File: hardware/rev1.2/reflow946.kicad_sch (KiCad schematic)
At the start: 47 parts, among them J1 VH-2A, J2 VH-3A2, J3 VH-3A2, J4 XH-A2, J5 HDR-M-2.54_2x3, Q1 BTA16-600BRG, Q2 MMBT3906, Q3 MMBT3906, Q4 MMBT3906, SW1 SW_Push, SW2 SW_Push, SW3 SW_Push, U1 MOC3041M, U2 ESP32-WROOM-32U, U3 MAX31855KASA, U4 AMS1117-3.3

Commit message: Fork to randware R2 variant
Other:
- company: Arnaud Durand -> Randware • Trent Rand

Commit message: rev2 schematic: J6 display pogo interface + J7 probe breakout
- Rename segment nets a/b -> SDA/SCL (IO17/IO22), trim dead tails
- J6 Conn_01x04 pogo target: 3V3/GND/SDA/SCL, R21/R22 4.7k pull-ups
- J7 Conn_01x06 breakout for external TC amp:
  CLK(IO14)/MISO(IO12) shared SPI, CS_EXT(IO4), TC_ADC(SENSOR_VP)
- Free IO4 & SENSOR_VP no-connects; DS1 7-seg -> DNP
- Remove orphaned a/b stubs, bus entries, dead DS1-side labels
- ERC: no new functional violations vs baseline; netlist verified
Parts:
- added J6: OLED_POGO, Connector_PinHeader_2.54mm:PinHeader_1x04_P2.54mm_Vertical, symbol Connector_Generic:Conn_01x04
- added J7: PROBE_BRK, Connector_PinHeader_2.54mm:PinHeader_1x06_P2.54mm_Vertical, symbol Connector_Generic:Conn_01x06
- added R21, R22: 4.7k, Resistor_SMD:R_0603_1608Metric_Pad0.98x0.95mm_HandSolder, symbol Device:R
- DS1: now not fitted
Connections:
- net +3.3V: now also J6.1 (Pin_1), J7.1 (Pin_1), R21.1, R22.1
- net CLK: now also J7.3 (Pin_3)
- net GND: now also J6.2 (Pin_2), J7.2 (Pin_2)
- net MISO: now also J7.4 (Pin_4)
- net CS_EXT: now reaches U2.26 (IO4)
- net CS_EXT: now also J7.5 (Pin_5)
- net TC_ADC: now reaches U2.4 (SENSOR_VP)
- net TC_ADC: now also J7.6 (Pin_6)
- net a: no longer names the net of R17.1
- net a: no longer U2.28 (IO17)
- net b: no longer names the net of R15.1
- net b: no longer U2.36 (IO22)
- new net SCL: J6.4 (Pin_4), R22.2, U2.36 (IO22)
- new net SDA: J6.3 (Pin_3), R21.2, U2.28 (IO17)

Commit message: rev2: J6 -> 8-pin TFT SPI header, embedded U6 second MAX31855 + EXT_TC terminal
Display path (ST7789V3 1.47in 172x320 IPS):
- J6 Conn_01x08: 3V3/GND/CS(IO23)/DC(IO16)/RST(IO13)/SCK(IO18)/MOSI(IO19)/BLK(IO5)
- Six freed segment GPIOs relabeled to TFT_* nets; dangling tails trimmed
- Q3 + R19 DNP to free IO18; DS1-side dead labels/stubs/bus entries removed

External probe subsystem:
- U6 MAX31855KASA clone sharing CLK/MISO, CS on IO4 (CS_EXT)
- J8 Phoenix MPT screw terminal + FB3/FB4 beads + C7 filter (mirrors U3 pattern)
- SENSOR_VP broken out as TC_ADC; J7 breakout retained

I2C expansion bus (IO17/IO22) kept with R21/R22 pull-ups.

ERC: zero new functional violations vs baseline (38 vs 49 findings;
net_not_bus_member improved). Netlist: all connectivity assertions pass,
including triac/button paths byte-identical to HEAD.
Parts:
- removed J6: OLED_POGO, Connector_PinHeader_2.54mm:PinHeader_1x04_P2.54mm_Vertical, symbol Connector_Generic:Conn_01x04
- added C7: 0.01u, Capacitor_SMD:C_0805_2012Metric_Pad1.18x1.45mm_HandSolder, symbol Device:C
- added FB3, FB4: FerriteBead, Resistor_SMD:R_0603_1608Metric_Pad0.98x0.95mm_HandSolder, symbol Device:FerriteBead
- added J6: TFT_1.47, Connector_PinHeader_2.54mm:PinHeader_1x08_P2.54mm_Vertical, symbol Connector_Generic:Conn_01x08
- added J8: EXT_TC, TerminalBlock_Phoenix:TerminalBlock_Phoenix_MPT-0,5-2-2.54_1x02_P2.54mm_Horizontal, symbol Connector_Generic:Conn_01x02
- added U6: MAX31855KASA, Package_SO:SOIC-8_3.9x4.9mm_P1.27mm, symbol Sensor_Temperature:MAX31855KASA
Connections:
- net +3.3V: now also J6.1 (Pin_1), U6.4 (VCC)
- net CLK: now also U6.5 (SCK)
- net CS_EXT: now also U6.6 (~{CS})
- net GND: now also J6.2 (Pin_2), U6.1 (GND)
- net MISO: now also U6.7 (SO)
- net c: no longer names the net of R13.1
- net c: no longer U2.31 (IO19)
- net d: no longer names the net of R11.1
- net d: no longer U2.27 (IO16)
- net d2: no longer names the net of R19.1
- net d2: no longer U2.30 (IO18)
- net dp: no longer names the net of R12.1
- net dp: no longer U2.29 (IO5)
- net f: no longer names the net of R16.1
- net f: no longer U2.37 (IO23)
- net g: no longer names the net of R14.1
- net g: no longer U2.16 (IO13)
- new net: C7.1, FB3.1, U6.3 (T+)
- new net: C7.2, FB4.1, U6.2 (T-)
- new net: FB3.2, J8.1 (Pin_1)
- new net: FB4.2, J8.2 (Pin_2)
- new net TFT_BLK: J6.8 (Pin_8), U2.29 (IO5)
- new net TFT_CS: J6.3 (Pin_3), U2.37 (IO23)
- new net TFT_DC: J6.4 (Pin_4), U2.27 (IO16)
- new net TFT_MOSI: J6.7 (Pin_7), U2.31 (IO19)
- new net TFT_RST: J6.5 (Pin_5), U2.16 (IO13)
- new net TFT_SCK: J6.6 (Pin_6), U2.30 (IO18)
- no-connect marks 11 -> 17

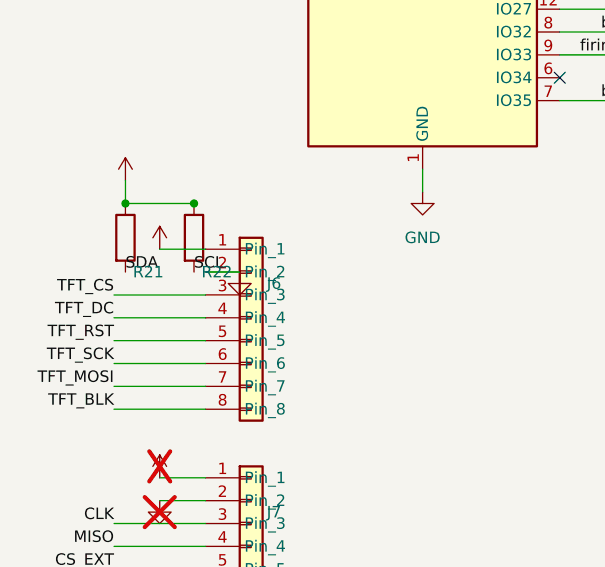
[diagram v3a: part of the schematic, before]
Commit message: rev2: route J6 GND stub leftward (was ending on connector body edge)
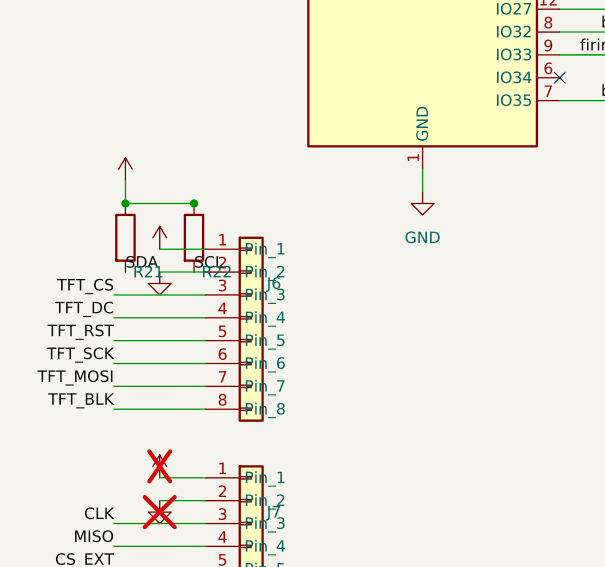
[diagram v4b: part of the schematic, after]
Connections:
- net SCL is gone; now on net GND: R22.2, U2.36 (IO22)
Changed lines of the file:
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@@
 	(wire
 		(pts
-			(xy 29.21 162.56) (xy 33.02 162.56)
+			(xy 29.21 162.56) (xy 24.13 162.56)
 		)
 		(stroke
@@
 	(symbol
 		(lib_id "power:GND")
-		(at 33.02 162.56 0)
+		(at 24.13 162.56 0)
 		(unit 1)
 		(body_style 1)
@@
 		)
 		(property "Footprint" ""
-			(at 33.02 162.56 0)
+			(at 24.13 162.56 0)
 			(hide yes)
 			(show_name no)
@@
 		)
 		(property "Datasheet" ""
-			(at 33.02 162.56 0)
+			(at 24.13 162.56 0)
 			(hide yes)
 			(show_name no)
@@
 		)
 		(property "Description" ""
-			(at 33.02 162.56 0)
+			(at 24.13 162.56 0)
 			(hide yes)
 			(show_name no)

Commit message: rev2: fix stray DNP flags on J7 power symbols; DNP Q3/R19 properly; relocate I2C pull-ups
- #PWR0118/#PWR0120 carried stray dnp=yes (collateral of an earlier
  unbounded rindex in the Q3/R19 DNP pass) -> cleared
- Q3 + R19 now genuinely DNP, freeing IO18 for TFT_SCK
- R21/R22 pull-up mini-circuit moved +21.59mm clear of J6's rail stubs
  (SCL label anchor previously sat on J6's GND stub path - nets verified
  separate but one edit away from shorting)
- ERC 38 (== baseline classes), netlist assertions all pass
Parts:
- Q3, R19: now not fitted
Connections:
- net GND: no longer R22.2, U2.36 (IO22)
- new net SCL: R22.2, U2.36 (IO22)
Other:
- moved on the sheet: R21, R22
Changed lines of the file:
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@@
 	)
 	(label "SDA"
-		(at 20.32 162.56 0)
+		(at 41.91 162.56 0)
 		(effects
 			(font
@@
 	)
 	(label "SCL"
-		(at 27.94 162.56 0)
+		(at 49.53 162.56 0)
 		(effects
 			(font
@@
 	(wire
 		(pts
-			(xy 20.32 152.4) (xy 20.32 154.94)
+			(xy 41.91 152.4) (xy 41.91 154.94)
 		)
 		(stroke
@@
 	(wire
 		(pts
-			(xy 20.32 154.94) (xy 27.94 154.94)
+			(xy 41.91 154.94) (xy 49.53 154.94)
 		)
 		(stroke
@@
 	)
 	(junction
-		(at 20.32 154.94)
+		(at 41.91 154.94)
 		(diameter 0)
 		(color 0 0 0 0)
 	)
 	(junction
-		(at 27.94 154.94)
+		(at 49.53 154.94)
 		(diameter 0)
 		(color 0 0 0 0)
@@
 		(on_board yes)
 		(in_pos_files yes)
-		(dnp no)
+		(dnp yes)
 		(property "Reference" "R19"
 			(at 180.34 33.02 90)
@@
 		(on_board yes)
 		(in_pos_files yes)
-		(dnp no)
+		(dnp yes)
 		(fields_autoplaced yes)
 		(property "Reference" "Q3"
@@
 	(symbol
 		(lib_id "Device:R")
-		(at 20.32 158.75 0)
+		(at 41.91 158.75 0)
 		(unit 1)
 		(body_style 1)
@@
 		(fields_autoplaced yes)
 		(property "Reference" "R21"
-			(at 22.86 162.56 0)
+			(at 44.45 162.56 0)
 			(show_name no)
 			(do_not_autoplace no)
@@
 		)
 		(property "Value" "4.7k"
-			(at 22.86 154.94 0)
+			(at 44.45 154.94 0)
 			(hide yes)
 			(show_name no)
@@
 		)
 		(property "Footprint" "Resistor_SMD:R_0603_1608Metric_Pad0.98x0.95mm_HandSolder"
-			(at 20.32 158.75 0)
+			(at 41.91 158.75 0)
 			(hide yes)
 			(show_name no)
@@
 		)
 		(property "Datasheet" "~"
-			(at 20.32 158.75 0)
+			(at 41.91 158.75 0)
 			(hide yes)
 			(show_name no)
@@
 		)
 		(property "Description" ""
-			(at 20.32 158.75 0)
+			(at 41.91 158.75 0)
 			(hide yes)
 			(show_name no)
@@
 	(symbol
 		(lib_id "Device:R")
-		(at 27.94 158.75 0)
+		(at 49.53 158.75 0)
 		(unit 1)
 		(body_style 1)
@@
 		(fields_autoplaced yes)
 		(property "Reference" "R22"
-			(at 30.48 162.56 0)
+			(at 52.07 162.56 0)
 			(show_name no)
 			(do_not_autoplace no)
@@
 		)
 		(property "Value" "4.7k"
-			(at 30.48 154.94 0)
+			(at 52.07 154.94 0)
 			(hide yes)
 			(show_name no)
@@
 		)
 		(property "Footprint" "Resistor_SMD:R_0603_1608Metric_Pad0.98x0.95mm_HandSolder"
-			(at 27.94 158.75 0)
+			(at 49.53 158.75 0)
 			(hide yes)
 			(show_name no)
@@
 		)
 		(property "Datasheet" "~"
-			(at 27.94 158.75 0)
+			(at 49.53 158.75 0)
 			(hide yes)
 			(show_name no)
@@
 		)
 		(property "Description" ""
-			(at 27.94 158.75 0)
+			(at 49.53 158.75 0)
 			(hide yes)
 			(show_name no)
@@
 	(symbol
 		(lib_id "power:+3.3V")
-		(at 20.32 152.4 0)
+		(at 41.91 152.4 0)
 		(unit 1)
 		(body_style 1)
@@
 		(fields_autoplaced yes)
 		(property "Reference" "#PWR0116"
-			(at 20.32 156.21 0)
+			(at 41.91 156.21 0)
 			(hide yes)
 			(show_name no)
@@
 		)
 		(property "Value" "+3.3V"
-			(at 20.32 147.32 0)
+			(at 41.91 147.32 0)
 			(hide yes)
 			(show_name no)
@@
 		)
 		(property "Footprint" ""
-			(at 20.32 152.4 0)
+			(at 41.91 152.4 0)
 			(hide yes)
 			(show_name no)
@@
 		)
 		(property "Datasheet" ""
-			(at 20.32 152.4 0)
+			(at 41.91 152.4 0)
 			(hide yes)
 			(show_name no)
@@
 		)
 		(property "Description" ""
-			(at 20.32 152.4 0)
+			(at 41.91 152.4 0)
 			(hide yes)
 			(show_name no)
@@
 		(on_board yes)
 		(in_pos_files yes)
-		(dnp yes)
+		(dnp no)
 		(fields_autoplaced yes)
 		(property "Reference" "#PWR0118"
@@
 		(on_board yes)
 		(in_pos_files yes)
-		(dnp yes)
+		(dnp no)
 		(fields_autoplaced yes)
 		(property "Reference" "#PWR0120"

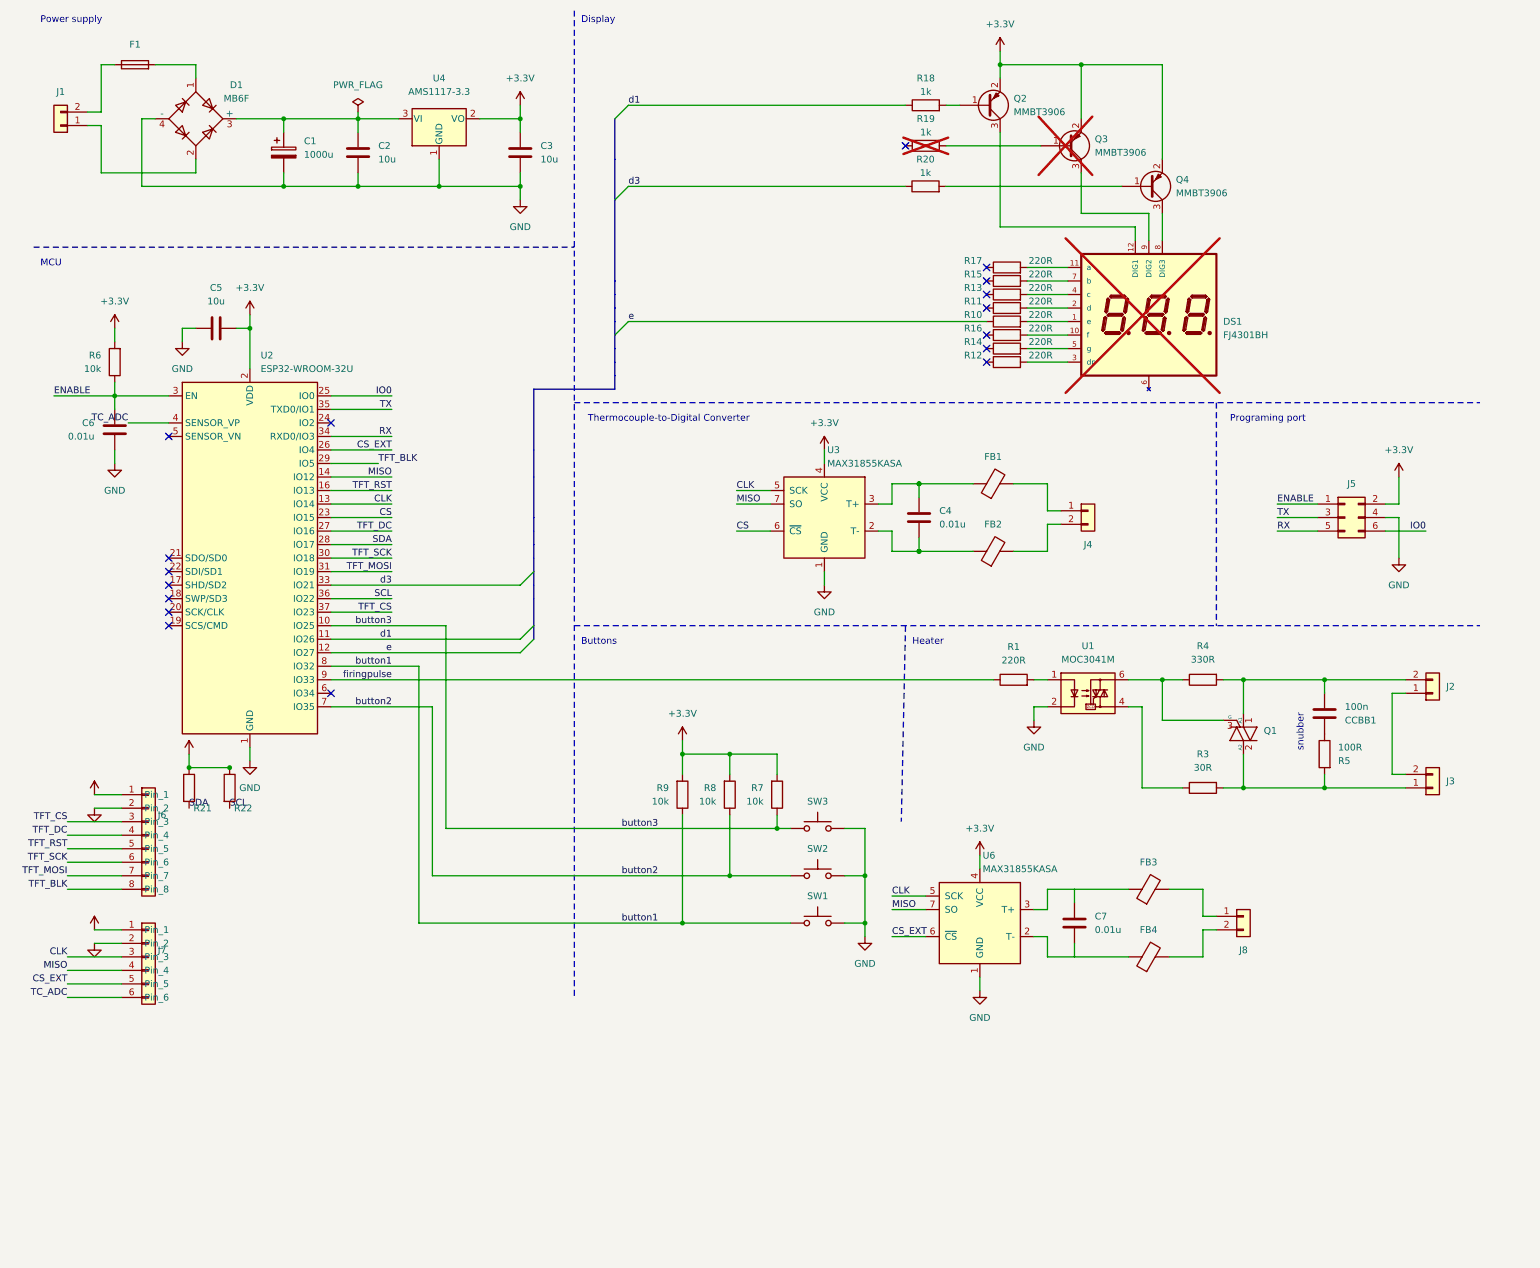
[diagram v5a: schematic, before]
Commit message: schematic: sheet cleanup — larger canvas, arranged, bordered (manual pass)
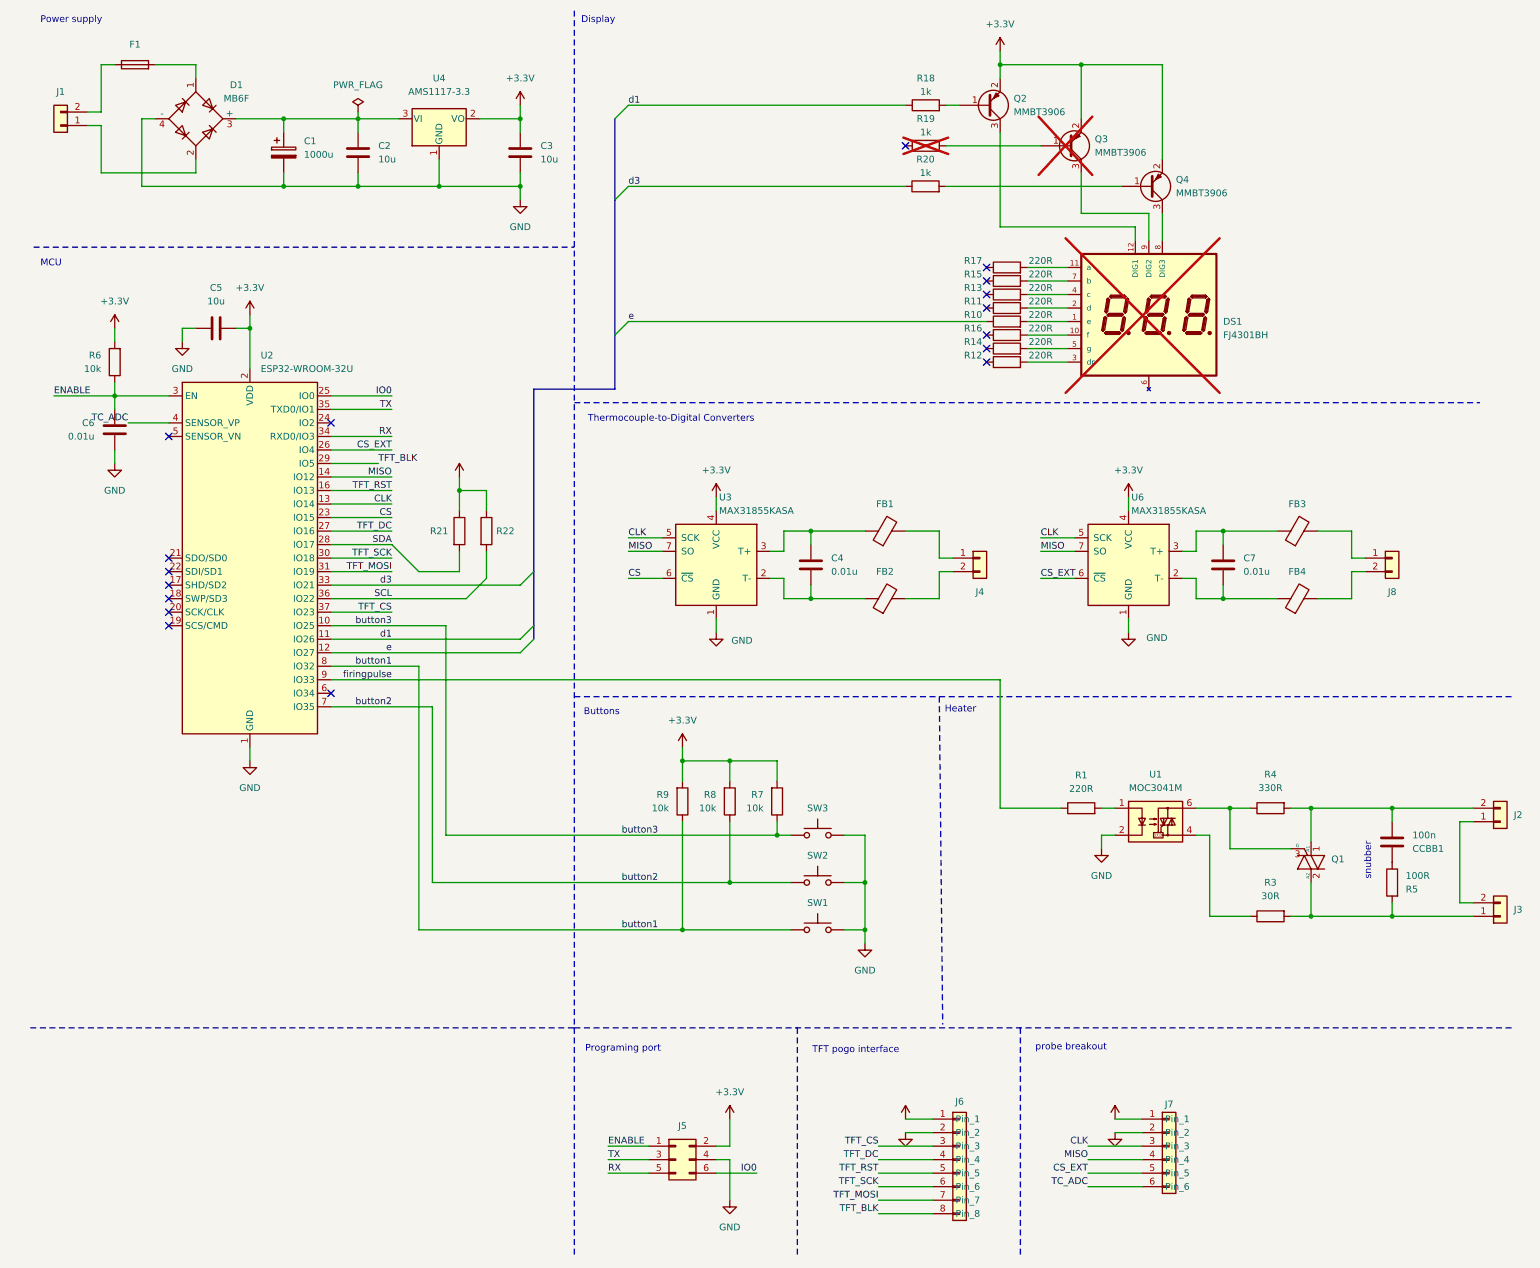
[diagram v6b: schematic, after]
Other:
- note added: "TFT pogo interface"
- note added: "Thermocouple-to-Digital Converters"
- note added: "probe breakout"
- note removed: "Thermocouple-to-Digital Converter"
- moved on the sheet: C4, C7, CCBB1, FB1, FB2, FB3, FB4, J2, J3, J4, J5, J6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
